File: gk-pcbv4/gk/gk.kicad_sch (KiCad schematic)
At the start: 4 parts

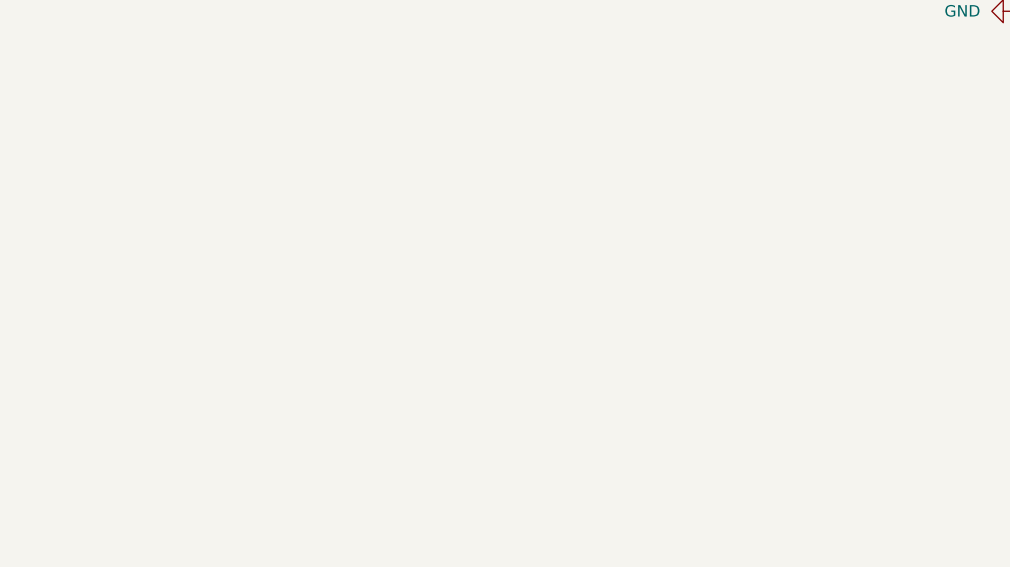
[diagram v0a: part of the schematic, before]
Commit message: add more errata
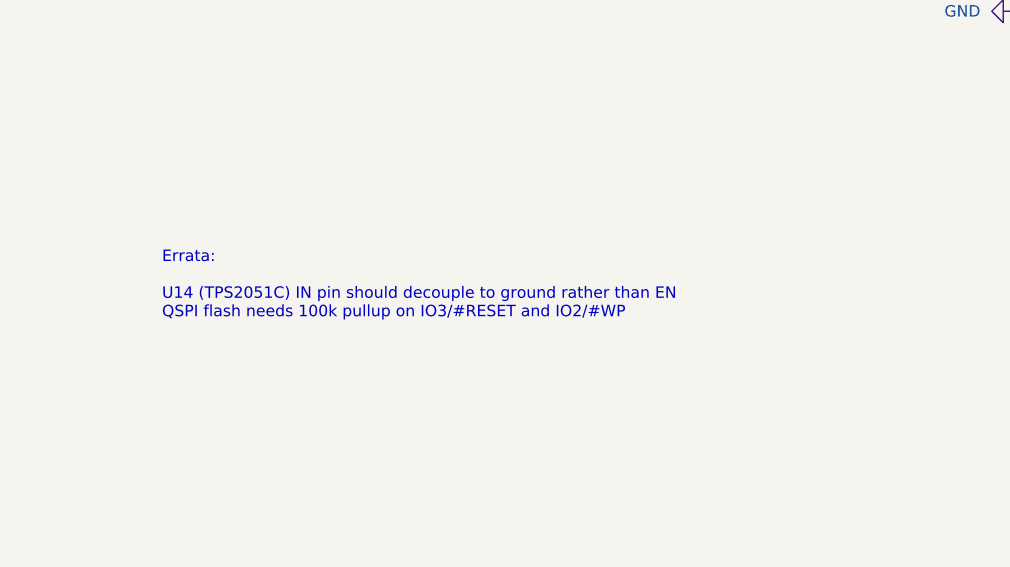
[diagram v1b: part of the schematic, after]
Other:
- note added: "Errata: U14 (TPS2051C) IN pin should decouple to ground rather than EN QSPI flash needs 100k pullup on IO3/#RESET and IO2/#WP"
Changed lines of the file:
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@@
+		)
+	)
+	(text "Errata:\n\nU14 (TPS2051C) IN pin should decouple to ground rather than EN\nQSPI flash needs 100k pullup on IO3/#RESET and IO2/#WP"
+		(exclude_from_sim no)
+		(at 104.648 80.01 0)
+		(effects
+			(font
+				(size 1.27 1.27)
+			)
+			(justify left)
 		)
 	)

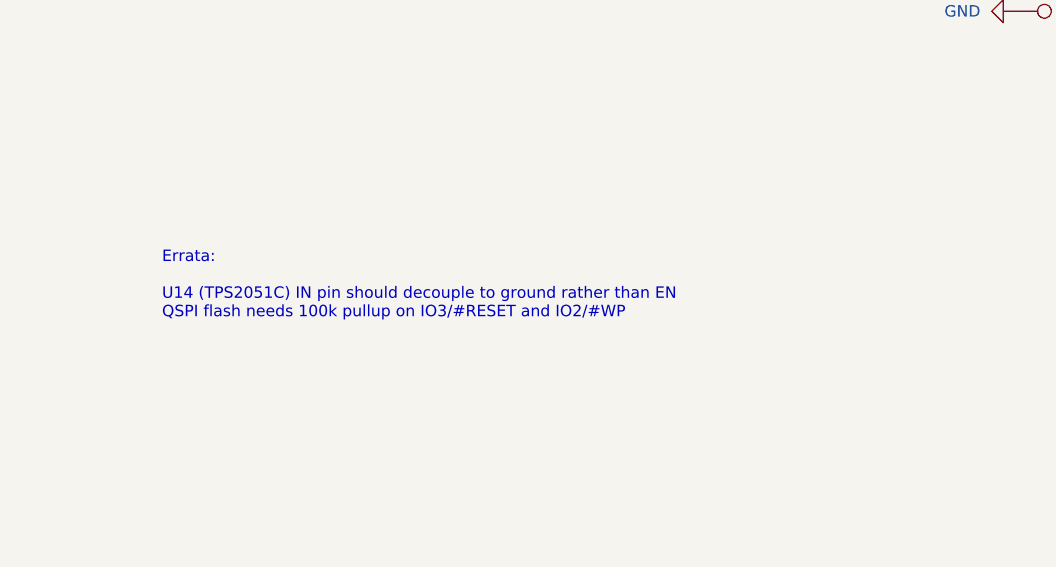
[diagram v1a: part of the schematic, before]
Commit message: add errata
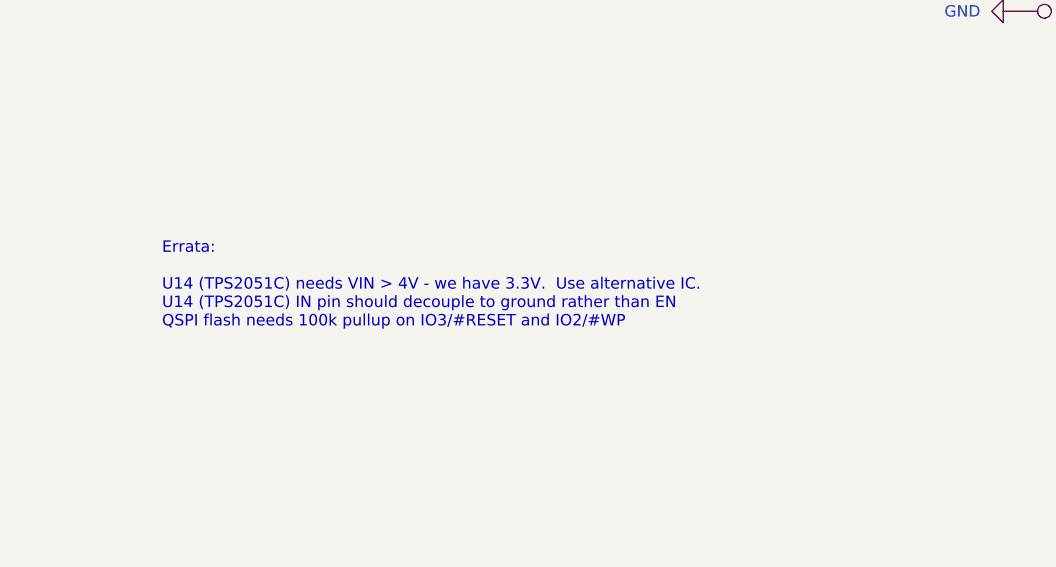
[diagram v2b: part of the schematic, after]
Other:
- note added: "Errata: U14 (TPS2051C) needs VIN > 4V - we have 3.3V. Use alternative IC. U14 (TPS2051C) IN pin should decouple to ground rather than EN QSPI flash needs 100k pullup on IO3/#RESET and IO2/#WP"
- note removed: "Errata: U14 (TPS2051C) IN pin should decouple to ground rather than EN QSPI flash needs 100k pullup on IO3/#RESET and IO2/#WP"
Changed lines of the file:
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@@
 		)
 	)
-	(text "Errata:\n\nU14 (TPS2051C) IN pin should decouple to ground rather than EN\nQSPI flash needs 100k pullup on IO3/#RESET and IO2/#WP"
+	(text "Errata:\n\nU14 (TPS2051C) needs VIN > 4V - we have 3.3V.  Use alternative IC.\nU14 (TPS2051C) IN pin should decouple to ground rather than EN\nQSPI flash needs 100k pullup on IO3/#RESET and IO2/#WP"
 		(exclude_from_sim no)
 		(at 104.648 80.01 0)

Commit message: update errata
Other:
- note added: "Errata: U14 (TPS2051C) needs VIN > 4V - we have 3.3V. Use alternative IC. - Can use, e.g. TPS2000EDBV or TPS2068EDBV with active low #EN. Add pull-up to +3V3, set MPU output as open-drain prior to enabling +3V3. U14 (TPS2051C) IN pin should decouple to ground rather than EN QSPI flash needs 100k pullup on IO3/#RESET and IO2/#WP"
- note removed: "Errata: U14 (TPS2051C) needs VIN > 4V - we have 3.3V. Use alternative IC. U14 (TPS2051C) IN pin should decouple to ground rather than EN QSPI flash needs 100k pullup on IO3/#RESET and IO2/#WP"
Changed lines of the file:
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@@
 		)
 	)
-	(text "Errata:\n\nU14 (TPS2051C) needs VIN > 4V - we have 3.3V.  Use alternative IC.\nU14 (TPS2051C) IN pin should decouple to ground rather than EN\nQSPI flash needs 100k pullup on IO3/#RESET and IO2/#WP"
+	(text "Errata:\n\nU14 (TPS2051C) needs VIN > 4V - we have 3.3V.  Use alternative IC.\n - Can use, e.g. TPS2000EDBV or TPS2068EDBV with active low #EN.\n    Add pull-up to +3V3, set MPU output as open-drain prior to enabling +3V3.\nU14 (TPS2051C) IN pin should decouple to ground rather than EN\nQSPI flash needs 100k pullup on IO3/#RESET and IO2/#WP"
 		(exclude_from_sim no)
 		(at 104.648 80.01 0)
